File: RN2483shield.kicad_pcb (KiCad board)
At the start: 2 copper layers, 68.9 x 53.6 mm, 8 parts, among them J1 SCREW_TERMINAL, J2 SMA, J3 SMA, P1 CONN_01X06, P2 CONN_01X06, P3 CONN_01X06, U1 RN2483

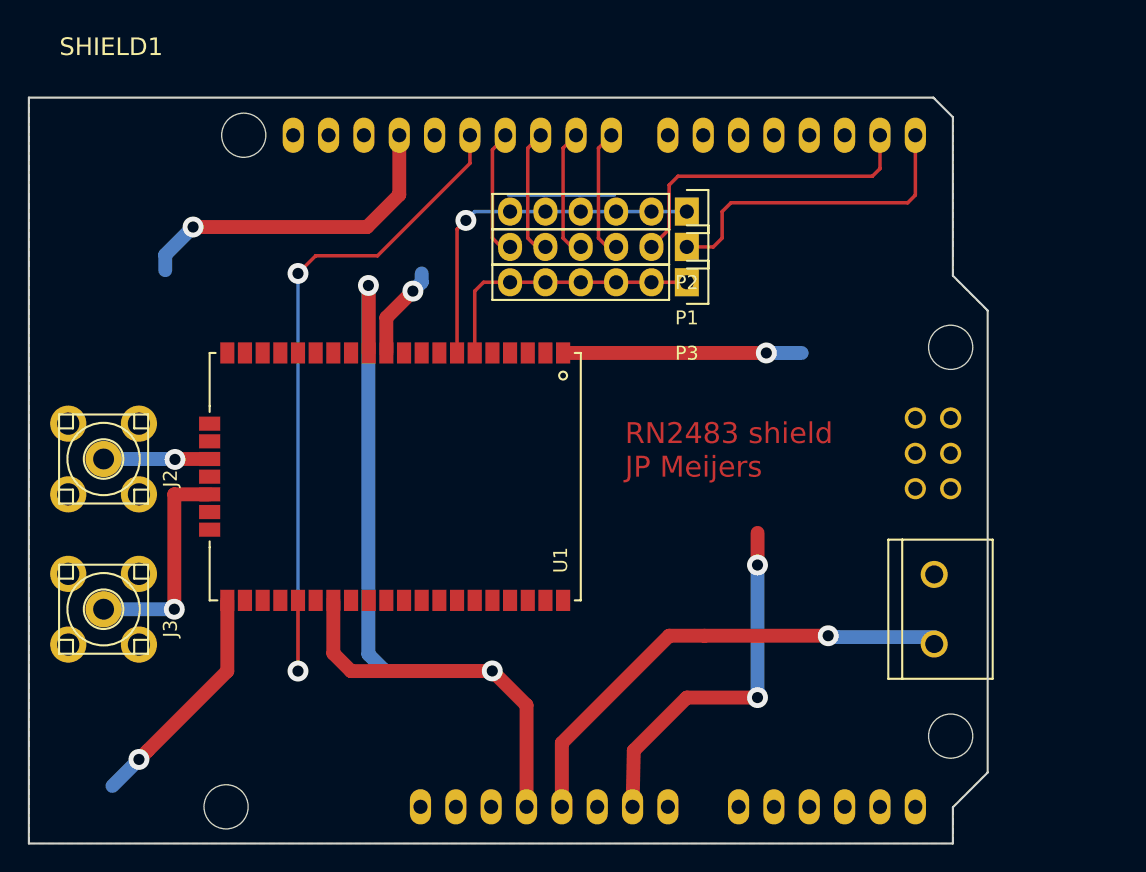
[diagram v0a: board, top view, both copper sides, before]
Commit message: redrafted the board with edgeSMA, gpio breakouts and solderpad serial connections
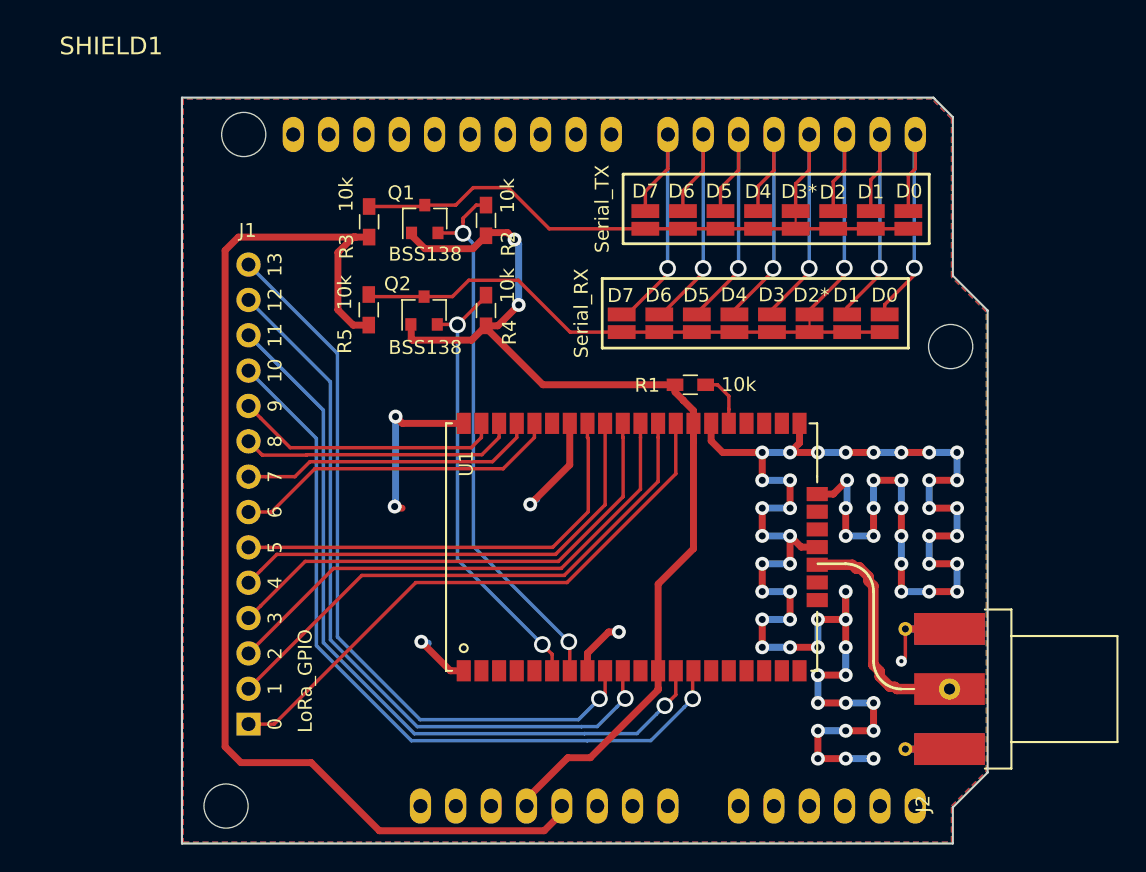
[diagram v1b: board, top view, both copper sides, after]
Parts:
- removed J3: SMA, MyFootprints:SMA_BOARD_UPRIGHT
- removed P1, P2, P3: CONN_01X06, Socket_Strips:Socket_Strip_Straight_1x06
- added D0: Jumper_NO_Small, MyFootprints:NO_SMD_JPR, F.Cu at (211.5, 60.9)
- added D0: Jumper_NO_Small, MyFootprints:NO_SMD_JPR, F.Cu at (209.8, 68.3)
- added D1: Jumper_NO_Small, MyFootprints:NO_SMD_JPR, F.Cu at (208.8, 60.9)
- added D1: Jumper_NO_Small, MyFootprints:NO_SMD_JPR, F.Cu at (207.1, 68.3)
- added D2: Jumper_NO_Small, MyFootprints:NO_SMD_JPR, F.Cu at (206.1, 60.9)
- added D2*: Jumper_NC_Small, MyFootprints:NC_SMD_JPR, F.Cu at (204.4, 68.3)
- added D3: Jumper_NO_Small, MyFootprints:NO_SMD_JPR, F.Cu at (201.7, 68.3)
- added D3*: Jumper_NC_Small, MyFootprints:NC_SMD_JPR, F.Cu at (203.4, 60.9)
- added D4: Jumper_NO_Small, MyFootprints:NO_SMD_JPR, F.Cu at (200.7, 60.9)
- added D4: Jumper_NO_Small, MyFootprints:NO_SMD_JPR, F.Cu at (199.0, 68.3)
- added D5: Jumper_NO_Small, MyFootprints:NO_SMD_JPR, F.Cu at (198.0, 60.9)
- added D5: Jumper_NO_Small, MyFootprints:NO_SMD_JPR, F.Cu at (196.3, 68.3)
- added D6: Jumper_NO_Small, MyFootprints:NO_SMD_JPR, F.Cu at (195.3, 60.9)
- added D6: Jumper_NO_Small, MyFootprints:NO_SMD_JPR, F.Cu at (193.6, 68.3)
- added D7: Jumper_NO_Small, MyFootprints:NO_SMD_JPR, F.Cu at (192.6, 60.9)
- added D7: Jumper_NO_Small, MyFootprints:NO_SMD_JPR, F.Cu at (190.9, 68.3)
- added Q1: BSS138, TO_SOT_Packages_SMD:SOT-23, F.Cu at (176.8, 60.2)
- added Q2: BSS138, TO_SOT_Packages_SMD:SOT-23, F.Cu at (176.7, 66.8)
- added R1: 10k, Resistors_SMD:R_0603_HandSoldering, F.Cu at (195.8, 72.1)
- added R2: 10k, Resistors_SMD:R_0603_HandSoldering, F.Cu at (181.2, 60.3)
- added R3: 10k, Resistors_SMD:R_0603_HandSoldering, F.Cu at (172.8, 60.4)
- added R4: 10k, Resistors_SMD:R_0603_HandSoldering, F.Cu at (181.2, 66.8)
- added R5: 10k, Resistors_SMD:R_0603_HandSoldering, F.Cu at (172.7, 66.8)
- J1: value SCREW_TERMINAL -> LoRa_GPIO; footprint freetronics_footprints:SCREWTERMINAL-5MM-2 -> MyFootprints:CONN_1x14
- J2: value SMA -> SMA_HF; footprint MyFootprints:SMA_BOARD_UPRIGHT -> MyFootprints:SMA_Edge
- SHIELD1: footprint freetronics_footprints:ARDUINO_SHIELD -> MyFootprints:ARDUINO_SHIELD_NOICSP
- U1: value RN2483 -> RN2483/RN2903
- moved J2 65.5 mm to (217.0, 94.0), turned to 270 degrees
- moved J1 50.0 mm to (164.1, 80.0), turned to 90 degrees
- moved U1 16.0 mm to (178.3, 74.9), turned to 270 degrees
- moved SHIELD1 0.05 mm to (148.5, 105.0)
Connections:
- net 3.3VOLT renamed +3V3
- J1 pad 1: GND -> GPIO_0
- J1 pad 2: BATTERY -> GPIO_1
- J2 pad 3: GND -> (no net)
- SHIELD1 pad 0: /HW_RX -> D0
- SHIELD1 pad 1: /HW_TX -> D1
- SHIELD1 pad 10: /AD_P10 -> (no net)
- SHIELD1 pad 11: /AD_P11 -> (no net)
- SHIELD1 pad 12: RN_RESET -> (no net)
- SHIELD1 pad 2: (no net) -> D2_RX
- SHIELD1 pad 3: (no net) -> D3_TX
- SHIELD1 pad 4: (no net) -> D4
- SHIELD1 pad 5: (no net) -> D5
- SHIELD1 pad 5V: BATTERY -> +5V
- SHIELD1 pad 6: (no net) -> D6
- SHIELD1 pad 7: (no net) -> D7
- SHIELD1 pad 8: /AD_P8 -> (no net)
- SHIELD1 pad 9: /AD_P9 -> (no net)
- U1 pad 10: (no net) -> GPIO_12
- U1 pad 13: (no net) -> GPIO_11
- U1 pad 14: (no net) -> GPIO_10
- U1 pad 32: RN_RESET -> Net-(R1-Pad1)
- U1 pad 35: (no net) -> GPIO_0
- U1 pad 36: (no net) -> GPIO_1
- U1 pad 37: (no net) -> GPIO_2
- U1 pad 38: (no net) -> GPIO_3
- U1 pad 39: (no net) -> GPIO_4
- U1 pad 40: (no net) -> GPIO_5
- U1 pad 43: (no net) -> GPIO_6
- U1 pad 44: (no net) -> GPIO_7
- U1 pad 45: (no net) -> GPIO_8
- U1 pad 46: (no net) -> GPIO_9
- U1 pad 6: UART_RADIO_TO_ARDUINO -> TX_RADIO
- U1 pad 7: UART_ARDUINO_TO_RADIO -> RX_RADIO
- U1 pad 9: (no net) -> GPIO_13
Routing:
- net +5V: track 0.00 -> 82.7 mm
- net GND: track 91.5 -> 162.9 mm, vias 6 -> 64
- net GPIO_11: track 0.00 -> 55.2 mm, vias 0 -> 1
- net GPIO_10: track 0.00 -> 54.9 mm, vias 0 -> 1
- net GPIO_12: track 0.00 -> 53.5 mm, vias 0 -> 1
- net GPIO_13: track 0.00 -> 53.5 mm, vias 0 -> 1
- net RN_RESET: track 51.3 -> 0.00 mm, vias 2 -> 0
- net GPIO_0: track 0.00 -> 41.8 mm
- net Net-(JP1-Pad1): track 0.00 -> 40.7 mm
- net GPIO_1: track 0.00 -> 39.8 mm
- net RX_RADIO: track 0.00 -> 39.5 mm, vias 0 -> 2
- net Net-(JP10-Pad1): track 0.00 -> 39.3 mm
- net GPIO_2: track 0.00 -> 37.8 mm
- net GPIO_3: track 0.00 -> 35.8 mm
- net BATTERY: track 34.5 -> 0.00 mm, vias 1 -> 0
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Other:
- board size 68.9 x 53.6 mm -> 57.9 x 53.6 mm
- net class Default: trace_width 1 -> 0.25; via_dia 1.5 -> 0.8; via_drill 0.8 -> 0.3
- net class PWR added: clearance 0.254, trace_width 0.5, via_dia 1, via_drill 0.5
- net class RADIO added: clearance 0.254, trace_width 0.75, via_dia 1.2, via_drill 0.8
- net class Thin removed
- board text added: "Serial_RX"
- board text added: "Serial_TX"
- board text removed: "RN2483 shield JP Meijers"

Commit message: and with title, link, revision and makers mark
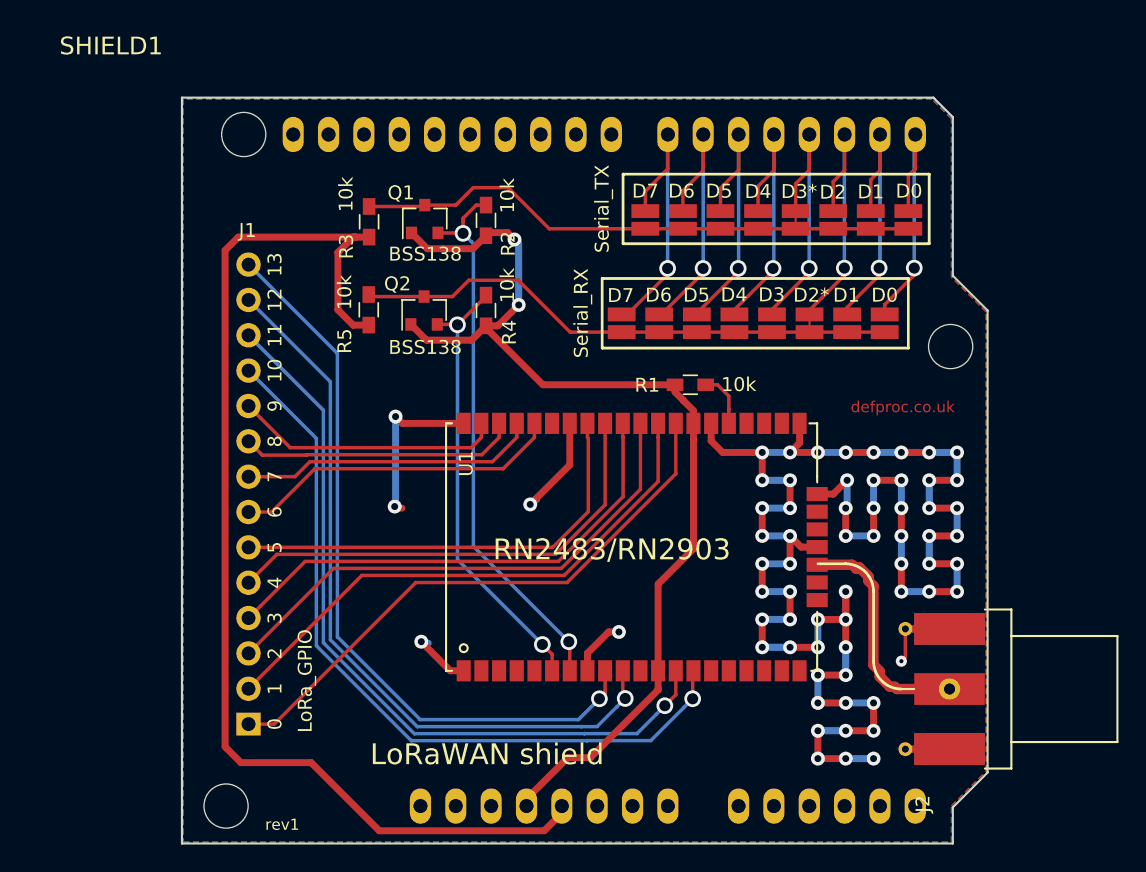
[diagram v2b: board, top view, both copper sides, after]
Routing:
- net +3V3: track 75.5 -> 74.8 mm
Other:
- board text added: "LoRaWAN shield"
- board text added: "RN2483/RN2903"
- board text added: "defproc.co.uk"
- board text added: "defproc.co.uk/p/LoRaWANshield"
- board text added: "rev1"
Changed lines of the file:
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@@
   (general
     (links 83)
-    (no_connects 1)
+    (no_connects 0)
     (area 141.952575 41 226.854001 105.454)
     (thickness 1.6)
-    (drawings 26)
-    (tracks 453)
+    (drawings 31)
+    (tracks 451)
     (zones 0)
     (modules 27)
@@
     (visible_elements FFFFEF7F)
     (pcbplotparams
-      (layerselection 0x01000_80000001)
+      (layerselection 0x010fc_80000001)
       (usegerberextensions true)
       (usegerberattributes true)
@@
       (linewidth 0.100000)
       (plotframeref true)
-      (viasonmask true)
+      (viasonmask false)
       (mode 1)
       (useauxorigin false)
@@
       (drillshape 0)
       (scaleselection 1)
-      (outputdirectory "test gerbers/"))
+      (outputdirectory gerbers/))
   )
   (net 0 "")
@@
     (pad 1 thru_hole circle (at 0 2.54 270) (size 1.524 1.524) (drill 0.8) (layers *.Cu *.Mask)
       (net 2 "Net-(J2-Pad1)"))
+  )
+  (gr_text defproc.co.uk/p/LoRaWANshield (at 186.7281 87.7951) (layer B.SilkS)
+    (effects (font (size 1 1) (thickness 0.2)) (justify mirror))
+  )
+  (gr_text rev1 (at 166.5097 103.7463) (layer F.SilkS)
+    (effects (font (size 0.8 0.8) (thickness 0.15)))
+  )
+  (gr_text "LoRaWAN shield" (at 181.229 98.7044) (layer F.SilkS)
+    (effects (font (size 1.5 1.5) (thickness 0.3)))
+  )
+  (gr_text defproc.co.uk (at 211.0994 73.7362) (layer F.Cu)
+    (effects (font (size 0.8 0.8) (thickness 0.15)))
+  )
+  (gr_text RN2483/RN2903 (at 190.1952 83.9851) (layer F.SilkS)
+    (effects (font (size 1.5 1.5) (thickness 0.3)))
   )
   (gr_line (start 211.5 64.5) (end 189.5 64.5) (layer F.SilkS) (width 0.2))
@@
   (segment (start 204.4 68.35) (end 207.1 68.35) (width 0.25) (layer F.Cu) (net 27))
   (segment (start 207.1 68.35) (end 209.8 68.35) (width 0.25) (layer F.Cu) (net 27))
+  (segment (start 181.15 61.425) (end 180.216473 62.358527) (width 0.5) (layer F.Cu) (net 28))
+  (segment (start 180.216473 62.358527) (end 176.933527 62.358527) (width 0.5) (layer F.Cu) (net 28))
+  (segment (start 176.933527 62.358527) (end 175.825 61.25) (width 0.5) (layer F.Cu) (net 28))
   (segment (start 175.825 61.25) (end 175.8 61.225) (width 0.5) (layer F.Cu) (net 28))
-  (segment (start 175.825 61.425) (end 175.825 61.25) (width 0.5) (layer F.Cu) (net 28))
-  (segment (start 176.758527 62.358527) (end 175.825 61.425) (width 0.5) (layer F.Cu) (net 28))
-  (segment (start 181.15 61.425) (end 180.216473 62.358527) (width 0.5) (layer F.Cu) (net 28))
-  (segment (start 180.216473 62.358527) (end 176.758527 62.358527) (width 0.5) (layer F.Cu) (net 28))
   (segment (start 181.15 67.9) (end 180.118897 68.931103) (width 0.5) (layer F.Cu) (net 28))
-  (segment (start 180.118897 68.931103) (end 175.856103 68.931103) (width 0.5) (layer F.Cu) (net 28))
-  (segment (start 175.775 68.85) (end 175.775 67.825) (width 0.5) (layer F.Cu) (net 28))
-  (segment (start 175.856103 68.931103) (end 175.775 68.85) (width 0.5) (layer F.Cu) (net 28))
+  (segment (start 180.118897 68.931103) (end 176.881103 68.931103) (width 0.5) (layer F.Cu) (net 28))
+  (segment (start 176.881103 68.931103) (end 175.775 67.825) (width 0.5) (layer F.Cu) (net 28))
   (segment (start 175.775 67.825) (end 175.75 67.8) (width 0.5) (layer F.Cu) (net 28))
   (segment (start 196.06 74.91) (end 196.06 73.994369) (width 0.5) (layer F.Cu) (net 28))
